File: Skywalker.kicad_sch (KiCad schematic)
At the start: 54 parts

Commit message: no message
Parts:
- removed Pn_Sol1, nO_Sol5: ~, symbol PID_symbols:Solenoid
- removed T2: ~, symbol PID_symbols:Tank
- added Pn_Sol?: ~, symbol PID_symbols:Pneumatic_Solenoid
- added nC_Sol?: ~, symbol PID_symbols:Normally_Closed_Solenoid
- renumbered EthBuffer to Ethanol, T1 to Ethanol, T1 to N2_Tank, G_Nitrous to Nitrous, T1 to Nitrous
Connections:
- net at N2_Tank.: now also CV5., PT?., Reg1., Reg2.
- net at Engine1.: now also PT1.; no longer PT3.
- net at PT1.: no longer Engine1.
- net at CV4.: now also Hose?.1
- net at Nitrous.: now also nC_Sol?.
- net at QD2.: now also CV6.
- new net: CV4., PT?., Pn_Sol?., Reg2., nO_Sol6., nO_Sol7.
- new net: CV4., Ethanol., MB_V2.
- new net: Engine1., PT3.
- new net: BV1., BV3., Engine1.
- new net: CV3., Ethanol., MB_V1., nO_Sol4.
- new net: CV4., nC_Sol?.
- new net: Burst_Disc1., CV1., Ethanol., PT2., SPRV1., nO_Sol1.
- new net: BV2., CV1., CV2.
- new net: Nitrous., PT?., nO_Sol2.
- new net: 3WayPBall?., Pn_Sol?.
- new net: 3WayPBall?., CV6., Nitrous.
- new net: BV1., Burst_Disc2., CV2., Nitrous., PT4., SPRV2.
- now unconnected: Burst_Disc1., Burst_Disc2., PT2., PT4., PT?., PT?., PT?.
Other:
- note added: "Buffer"
- note added: "Gaseous"
- note added: "Main"
- moved on the sheet: N2_Tank, PT?

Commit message: update
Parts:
- gave numbers to parts that had none: 13
- renumbered BV1 to BV2, BV2 to BV3, BV3 to BV4, BV1 to BV5, CV6 to CV10, CV1 to CV3, CV2 to CV4, CV3 to CV5, CV4 to CV6, CV3 to CV7, CV4 to CV8, CV5 to CV9, Ethanol to Fuel1, Ethanol to Ig_Fuel1, Nitrous to Ig_Ox1, MB_V1 to MB_V2, MB_V2 to MB_V3, N2_Tank to N2_Tank1, Nitrous to Ox1, PT4 to PT10, PT1 to PT5, PT2 to PT6, PT3 to PT9, nO_Sol6 to nO_Sol5, nO_Sol7 to nO_Sol6
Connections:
- net at N2_Tank1.: now also CV9., PT7., Reg1., Reg2.
- net at Engine1.: now also PT5.; no longer PT9.
- net at PT5.: no longer Engine1.
- net at CV8.: now also Hose4.1; no longer nC_Sol1.
- net at QD2.: now also CV10.
- new net: CV6., PT13., Pn_Sol1., Reg2., nO_Sol5., nO_Sol6.
- new net: CV6., Ig_Fuel1., MB_V3.
- new net: Engine1., PT9.
- new net: BV2., BV4., Engine1.
- new net: CV5., Ig_Fuel1., MB_V2., nO_Sol4.
- new net: CV8., nC_Sol1.
- new net: Burst_Disc1., CV3., Fuel1., PT6., SPRV1., nO_Sol1.
- new net: BV3., CV3., CV4.
- new net: Ig_Ox1., PT12., nO_Sol2.
- new net: 3WayPBall1., CV10., Ox1.
- new net: BV5., Burst_Disc2., CV4., Ox1., PT10., SPRV2.
- now unconnected: Burst_Disc1., Burst_Disc2., PT10., PT12., PT13., PT6., PT7.

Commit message: legend
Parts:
- removed MB_V1: ~, symbol PID_symbols:MBallValve
- removed Pn_Sol1: ~, symbol PID_symbols:Pneumatic_Solenoid
- added MB_V?: ~, symbol PID_symbols:MBallValve
- added Pn_Sol?: ~, symbol PID_symbols:Pneumatic_Solenoid
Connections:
- net at N2_Tank1.: now also CV9., PT7., Reg1., Reg2.
- net at Engine1.: now also PT5.; no longer PT9.
- net at PT5.: no longer Engine1.
- net at CV8.: now also Hose4.1; no longer nC_Sol1.
- net at CV5., Fuel1., Hose1.1: now also MB_V?.
- net at QD2.: now also CV10.
- new net: CV6., PT13., Pn_Sol?., Reg2., nO_Sol5., nO_Sol6.
- new net: CV6., Ig_Fuel1., MB_V3.
- new net: Engine1., PT9.
- new net: BV2., BV4., Engine1.
- new net: CV5., Ig_Fuel1., MB_V2., nO_Sol4.
- new net: CV8., nC_Sol1.
- new net: Burst_Disc1., CV3., Fuel1., PT6., SPRV1., nO_Sol1.
- new net: BV3., CV3., CV4.
- new net: Ig_Ox1., PT12., nO_Sol2.
- new net: 3WayPBall1., Pn_Sol?.
- new net: 3WayPBall1., CV10., Ox1.
- new net: BV5., Burst_Disc2., CV4., Ox1., PT10., SPRV2.
- now unconnected: Burst_Disc1., Burst_Disc2., PT10., PT12., PT13., PT6., PT7.
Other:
- note added: "1/2" Pipe"
- note added: "1/4" Pipe"
- note added: "LEGEND"
- note added: "Tubing"
- moved on the sheet: Burst_Disc1, CV7, CV8, Hose3, Hose4, PT11, T_I1, nC_Sol1, nO_Sol4

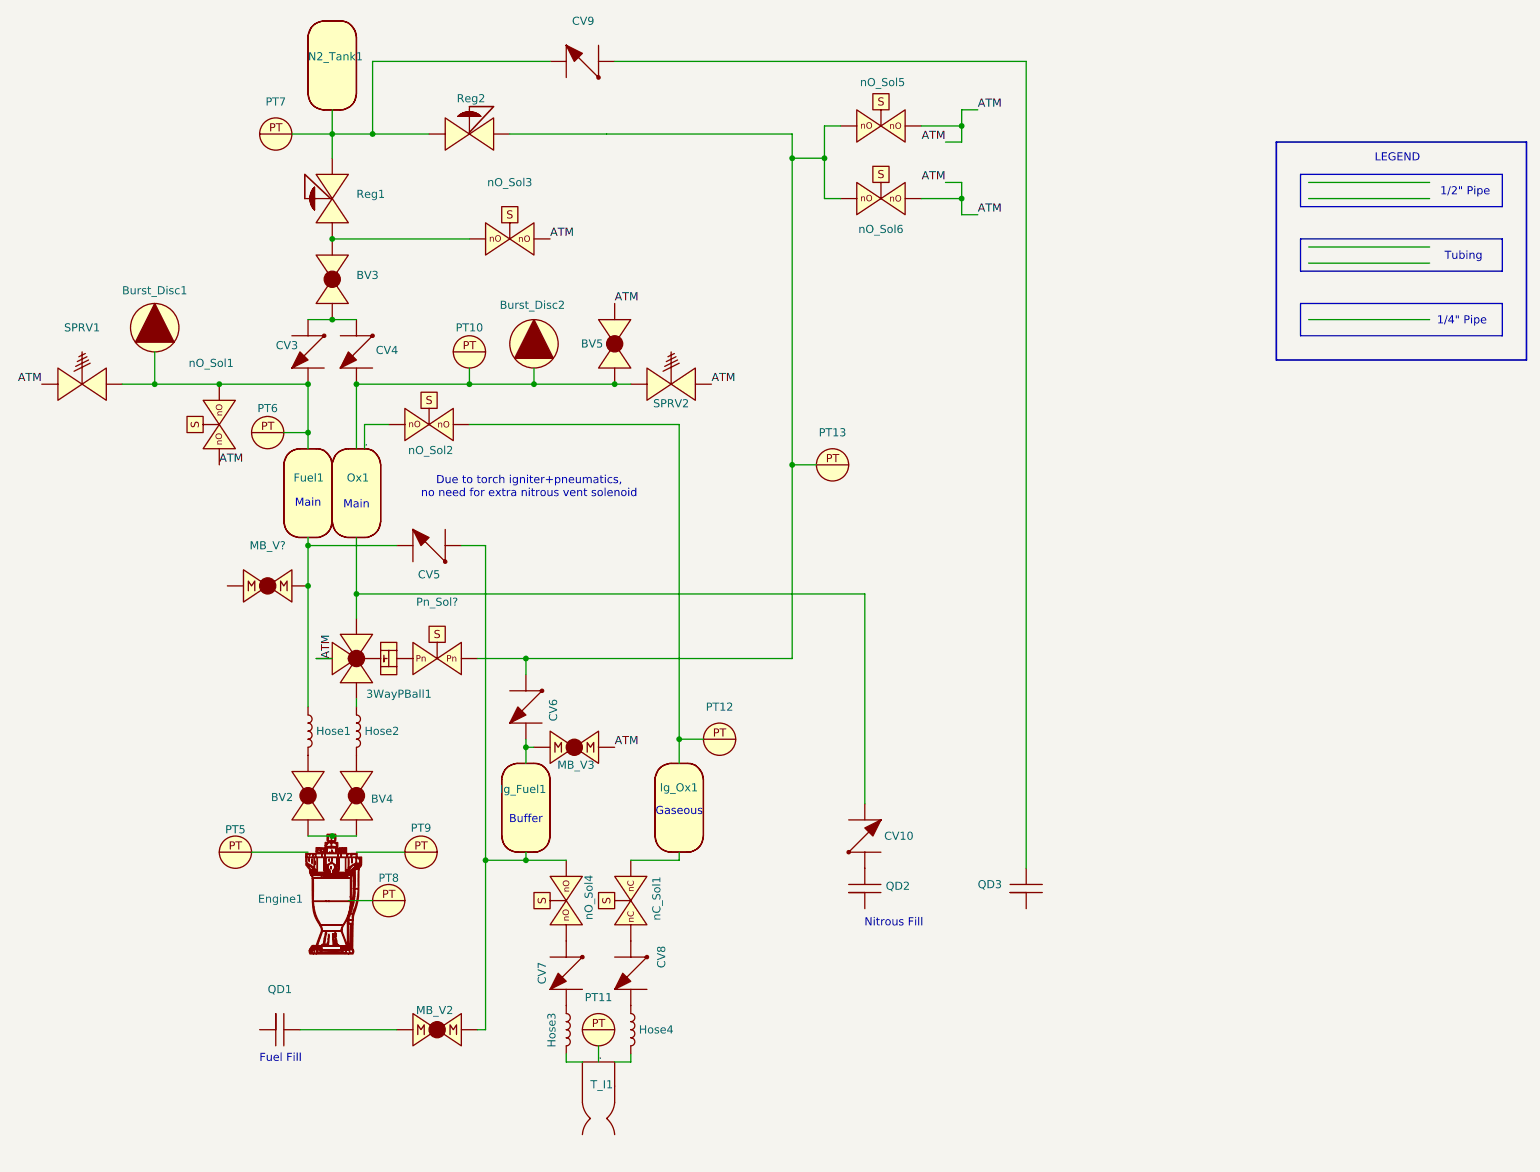
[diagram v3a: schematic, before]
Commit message: added L9 P&ID from Babs, he had problems using git
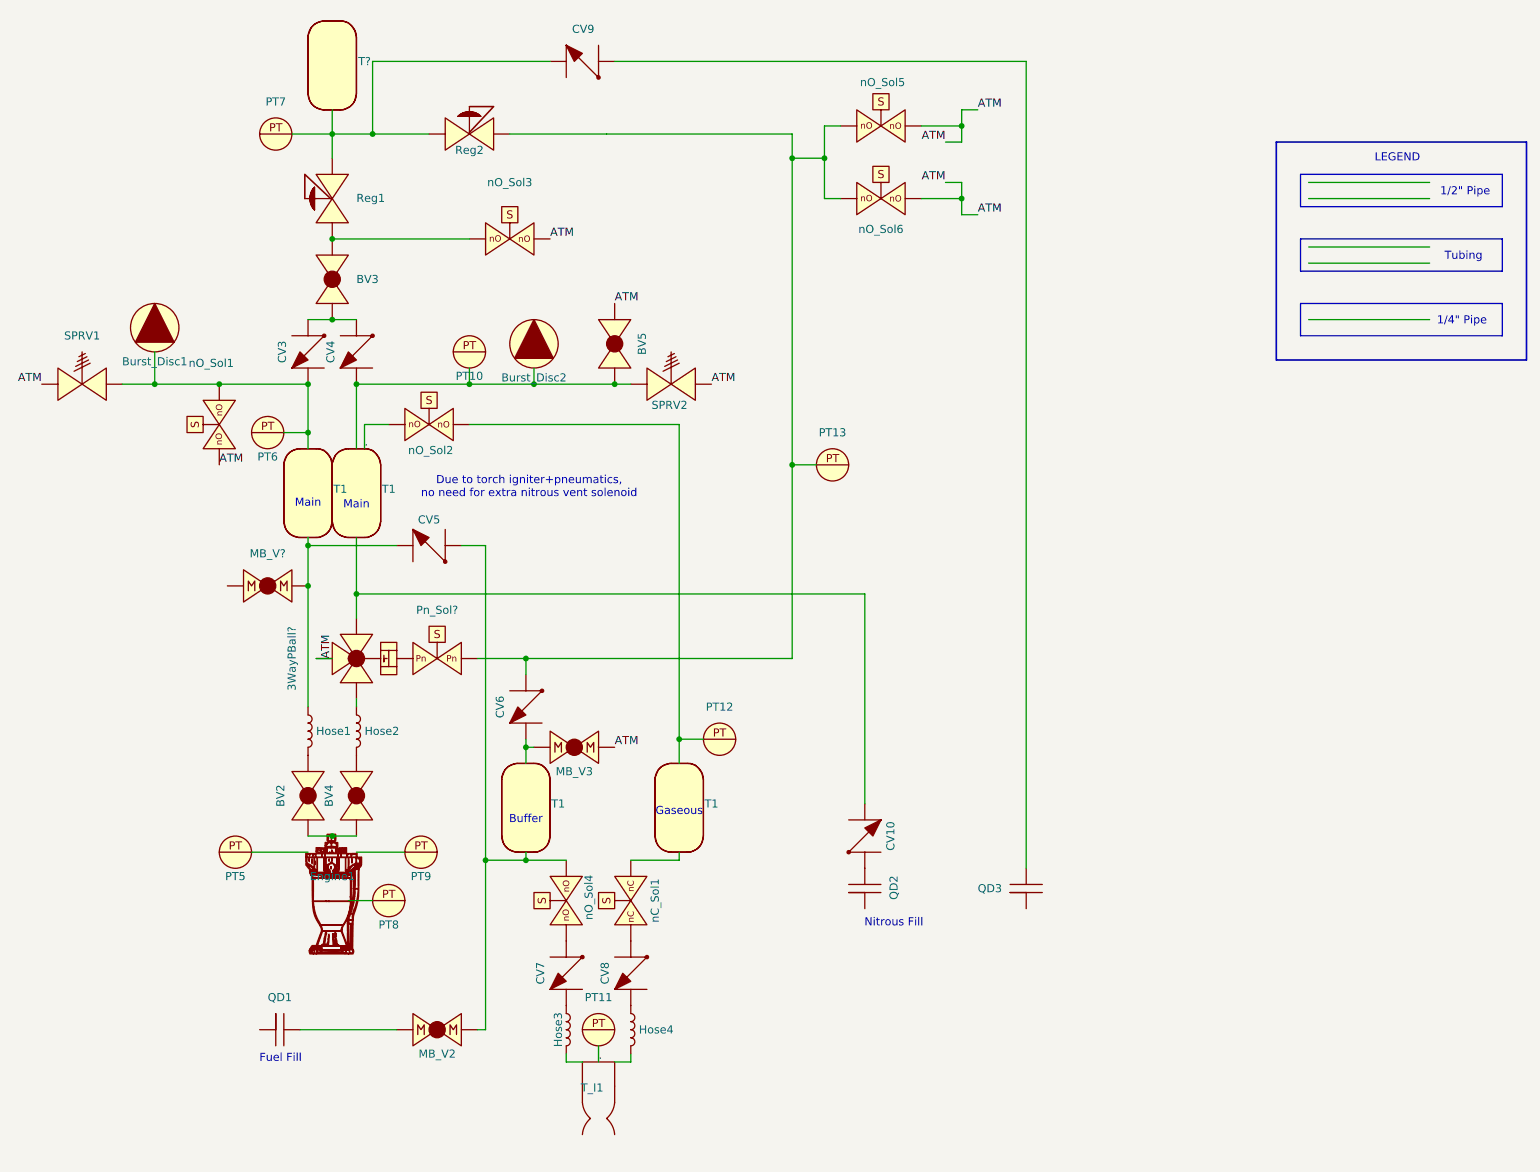
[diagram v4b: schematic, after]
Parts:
- 3WayPBall?: renamed from 3WayPBall1; value ~ -> (none)
- BV2, BV3, BV4, BV5, Burst_Disc1, Burst_Disc2, CV10, CV3, CV4, CV5, CV6, CV7, CV8, CV9, Engine1, Hose1, Hose2, Hose3, Hose4, MB_V2, MB_V3, MB_V?, PT10, PT11, PT12, PT13, PT5, PT6, PT7, PT8, PT9, Pn_Sol?, QD1, QD2, QD3, Reg1, Reg2, SPRV1, SPRV2, T_I1, nC_Sol1: value ~ -> (none)
- T1: renamed from Ig_Fuel1; value ~ -> (none)
- T1: renamed from Ig_Ox1; value ~ -> (none)
- T1: renamed from Fuel1; value ~ -> (none)
- T1: renamed from Ox1; value ~ -> (none)
- T?: renamed from N2_Tank1; value ~ -> (none)
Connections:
- net at T?.: now also CV9., PT7., Reg1., Reg2.
- net at Engine1.: now also PT5.; no longer PT9.
- net at PT5.: no longer Engine1.
- net at CV8.: now also Hose4.1; no longer nC_Sol1.
- net at QD2.: now also CV10.
- new net: CV6., PT13., Pn_Sol?., Reg2., nO_Sol5., nO_Sol6.
- new net: CV6., MB_V3., T1.
- new net: Engine1., PT9.
- new net: BV2., BV4., Engine1.
- new net: CV5., MB_V2., T1., nO_Sol4.
- new net: CV8., nC_Sol1.
- new net: Burst_Disc1., CV3., PT6., SPRV1., T1., nO_Sol1.
- new net: BV3., CV3., CV4.
- new net: PT12., T1., nO_Sol2.
- new net: 3WayPBall?., CV10., T1.
- new net: BV5., Burst_Disc2., CV4., PT10., SPRV2., T1.
- now unconnected: Burst_Disc1., Burst_Disc2., PT10., PT12., PT13., PT6., PT7.

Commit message: okokok
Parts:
- 3WayPBall1: renamed from 3WayPBall?; value (none) -> ~
- BV2, BV3, BV4, BV5, Burst_Disc1, Burst_Disc2, CV10, CV3, CV4, CV5, CV6, CV7, Engine1, Hose1, Hose2, Hose3, Hose4, MB_V2, MB_V3, PT10, PT11, PT12, PT13, PT5, PT6, PT7, PT8, PT9, QD1, QD2, QD3, Reg1, Reg2, SPRV1, SPRV2, T_I1, nC_Sol1: value (none) -> ~
- CV8: renamed from CV9; value (none) -> ~
- CV9: renamed from CV8; value (none) -> ~
- Fuel, Ox: renamed from T1; value (none) -> ~
- MB_V1: renamed from MB_V?; value (none) -> ~
- N1: renamed from T?; value (none) -> ~
- Pn_Sol1: renamed from Pn_Sol?; value (none) -> ~
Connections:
- net at N1.: now also CV8., PT7., Reg1., Reg2.
- net at Engine1.: now also PT5.; no longer PT9.
- net at PT5.: no longer Engine1.
- net at CV9.: now also Hose4.1; no longer nC_Sol1.
- net at QD2.: now also CV10.
- new net: CV6., PT13., Pn_Sol1., Reg2., nO_Sol5., nO_Sol6.
- new net: CV6., Fuel., MB_V3.
- new net: Engine1., PT9.
- new net: BV2., BV4., Engine1.
- new net: CV5., Fuel., MB_V2., nO_Sol4.
- new net: CV9., nC_Sol1.
- new net: Burst_Disc1., CV3., Fuel., PT6., SPRV1., nO_Sol1.
- new net: BV3., CV3., CV4.
- new net: Ox., PT12., nO_Sol2.
- new net: 3WayPBall1., CV10., Ox.
- new net: BV5., Burst_Disc2., CV4., Ox., PT10., SPRV2.
- now unconnected: Burst_Disc1., Burst_Disc2., PT10., PT12., PT13., PT6., PT7.
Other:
- note removed: "1/2" Pipe"
- note removed: "1/4" Pipe"
- note removed: "LEGEND"
- note removed: "Tubing"
- moved on the sheet: Burst_Disc2, PT10

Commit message: no message
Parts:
- renumbered Fuel to Fuel1, Fuel to Fuel2, Ox to Ox1, Ox to Ox2
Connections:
- net at N1.: now also CV8., PT7., Reg1., Reg2.
- net at Engine1.: now also PT5.; no longer PT9.
- net at PT5.: no longer Engine1.
- net at CV9.: now also Hose4.1; no longer nC_Sol1.
- net at QD2.: now also CV10.
- new net: CV6., PT13., Pn_Sol1., Reg2., nO_Sol5., nO_Sol6.
- new net: CV6., Fuel2., MB_V3.
- new net: Engine1., PT9.
- new net: BV2., BV4., Engine1.
- new net: CV5., Fuel2., MB_V2., nO_Sol4.
- new net: CV9., nC_Sol1.
- new net: Burst_Disc1., CV3., Fuel1., PT6., SPRV1., nO_Sol1.
- new net: BV3., CV3., CV4.
- new net: Ox2., PT12., nO_Sol2.
- new net: 3WayPBall1., CV10., Ox1.
- new net: BV5., Burst_Disc2., CV4., Ox1., PT10., SPRV2.
- now unconnected: Burst_Disc1., Burst_Disc2., PT10., PT12., PT13., PT6., PT7.
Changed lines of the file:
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@@
 		(on_board yes)
 		(dnp no)
-		(property "Reference" "Fuel"
+		(property "Reference" "Fuel2"
 			(at 93.726 138.43 0)
 			(effects
@@
 			(project "P_IDs"
 				(path "/045f1f05-3134-4b6d-91b6-463031104f1e/8ff5724e-b29b-49c2-a1fa-190081404476"
-					(reference "Fuel")
+					(reference "Fuel2")
 					(unit 1)
 				)
@@
 		(on_board yes)
 		(dnp no)
-		(property "Reference" "Ox"
+		(property "Reference" "Ox2"
 			(at 116.84 138.176 0)
 			(effects
@@
 			(project "P_IDs"
 				(path "/045f1f05-3134-4b6d-91b6-463031104f1e/8ff5724e-b29b-49c2-a1fa-190081404476"
-					(reference "Ox")
+					(reference "Ox2")
 					(unit 1)
 				)
@@
 		(on_board yes)
 		(dnp no)
-		(property "Reference" "Fuel"
+		(property "Reference" "Fuel1"
 			(at 59.182 88.646 0)
 			(effects
@@
 			(project "P_IDs"
 				(path "/045f1f05-3134-4b6d-91b6-463031104f1e/8ff5724e-b29b-49c2-a1fa-190081404476"
-					(reference "Fuel")
+					(reference "Fuel1")
 					(unit 1)
 				)
@@
 		(on_board yes)
 		(dnp no)
-		(property "Reference" "Ox"
+		(property "Reference" "Ox1"
 			(at 67.31 88.646 0)
 			(effects
@@
 			(project "P_IDs"
 				(path "/045f1f05-3134-4b6d-91b6-463031104f1e/8ff5724e-b29b-49c2-a1fa-190081404476"
-					(reference "Ox")
-					(unit 1)
-				)
+					(reference "Ox1")
+					(unit 1)
+				)

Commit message: no message
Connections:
- net at N1.: now also CV8., PT7., Reg1., Reg2.
- net at Engine1.: now also PT5.; no longer PT9.
- net at PT5.: no longer Engine1.
- net at CV9.: now also Hose4.1; no longer nC_Sol1.
- net at QD2.: now also CV10.
- new net: CV6., PT13., Pn_Sol1., Reg2., nO_Sol5., nO_Sol6.
- new net: CV6., Fuel2., MB_V3.
- new net: Engine1., PT9.
- new net: BV2., BV4., Engine1.
- new net: CV5., Fuel2., MB_V2., nO_Sol4.
- new net: CV9., nC_Sol1.
- new net: Burst_Disc1., CV3., Fuel1., PT6., SPRV1., nO_Sol1.
- new net: BV3., CV3., CV4.
- new net: Ox2., PT12., nO_Sol2.
- new net: 3WayPBall1., CV10., Ox1.
- new net: BV5., Burst_Disc2., CV4., Ox1., PT10., SPRV2.
- now unconnected: Burst_Disc1., Burst_Disc2., PT10., PT12., PT13., PT6., PT7.
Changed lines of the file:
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@@
 	(wire
 		(pts
+			(xy 87.63 148.59) (xy 93.98 148.59)
+		)
+		(stroke
+			(width 0)
+			(type solid)
+			(color 255 255 255 1)
+		)
+	)
+	(wire
+		(pts
 			(xy 100.33 148.59) (xy 93.98 148.59)
 		)
@@
 	(wire
 		(pts
-			(xy 87.63 148.59) (xy 93.98 148.59)
-		)
-		(stroke
-			(width 0)
-			(type solid)
-			(color 255 255 255 1)
-		)
-	)
-	(wire
-		(pts
 			(xy 140.97 33.02) (xy 143.51 33.02)
 		)
@@
 	)
 	(symbol
-		(lib_name "PID_symbols:Tank")
 		(lib_id "PID_symbols:Tank")
 		(at 62.23 27.94 0)
@@
 	)
 	(symbol
-		(lib_name "PID_symbols:Check_Valve")
 		(lib_id "PID_symbols:Check_Valve")
 		(at 93.98 121.92 270)
@@
 	)
 	(symbol
-		(lib_name "PID_symbols:Pressure_Transducer")
 		(lib_id "PID_symbols:Pressure_Transducer")
 		(at 72.39 154.94 0)
@@
 	)
 	(symbol
-		(lib_name "PID_symbols:Pressure_Transducer")
 		(lib_id "PID_symbols:Pressure_Transducer")
 		(at 77.47 147.32 0)
@@
 	)
 	(symbol
-		(lib_name "PID_symbols:Check_Valve")
 		(lib_id "PID_symbols:Check_Valve")
 		(at 105.41 22.86 180)
@@
 	)
 	(symbol
-		(lib_name "PID_symbols:MBallValve")
 		(lib_id "PID_symbols:MBallValve")
 		(at 80.01 175.26 0)
@@
 	)
 	(symbol
-		(lib_name "PID_symbols:Ball_Valve")
 		(lib_id "PID_symbols:Ball_Valve")
 		(at 67.31 134.62 270)
@@
 	)
 	(symbol
-		(lib_name "PID_symbols:Check_Valve")
 		(lib_id "PID_symbols:Check_Valve")
 		(at 110.49 163.83 270)
@@
 	)
 	(symbol
-		(lib_name "PID_symbols:Check_Valve")
 		(lib_id "PID_symbols:Check_Valve")
 		(at 59.69 66.04 270)
@@
 	)
 	(symbol
-		(lib_name "PID_symbols:Pressure_Regulator")
 		(lib_id "PID_symbols:Pressure_Regulator")
 		(at 81.28 34.29 0)
@@
 	)
 	(symbol
-		(lib_name "PID_symbols:Pressure_Transducer")
 		(lib_id "PID_symbols:Pressure_Transducer")
 		(at 53.34 81.28 0)
@@
 	)
 	(symbol
-		(lib_name "PID_symbols:Tank")
 		(lib_id "PID_symbols:Tank")
 		(at 92.71 144.78 0)
@@
 	)
 	(symbol
-		(lib_name "PID_symbols:Tank")
 		(lib_id "PID_symbols:Tank")
 		(at 116.84 144.78 0)
@@
 	)
 	(symbol
-		(lib_name "PID_symbols:Check_Valve")
 		(lib_id "PID_symbols:Check_Valve")
 		(at 100.33 163.83 270)
@@
 	)
 	(symbol
-		(lib_name "PID_symbols:Tank")
 		(lib_id "PID_symbols:Tank")
 		(at 58.42 95.25 0)
@@
 	)
 	(symbol
-		(lib_name "PID_symbols:Pressure_Transducer")
 		(lib_id "PID_symbols:Pressure_Transducer")
 		(at 48.26 147.32 0)
@@
 	)
 	(symbol
-		(lib_name "PID_symbols:Solenoid")
 		(lib_id "PID_symbols:Solenoid")
 		(at 146.05 33.02 0)
@@
 	)
 	(symbol
-		(lib_name "PID_symbols:Quick_Disconnect")
 		(lib_id "PID_symbols:Quick_Disconnect")
 		(at 172.72 153.67 90)
@@
 	)
 	(symbol
-		(lib_name "PID_symbols:Ball_Valve")
 		(lib_id "PID_symbols:Ball_Valve")
 		(at 107.95 71.12 90)
@@
 	)
 	(symbol
-		(lib_name "PID_symbols:Solenoid")
 		(lib_id "PID_symbols:Solenoid")
 		(at 74.93 80.01 0)
@@
 	)
 	(symbol
-		(lib_name "PID_symbols:Quick_Disconnect")
 		(lib_id "PID_symbols:Quick_Disconnect")
 		(at 54.61 175.26 0)
@@
 	)
 	(symbol
-		(lib_name "PID_symbols:Quick_Disconnect")
 		(lib_id "PID_symbols:Quick_Disconnect")
 		(at 147.32 153.67 90)
@@
 	)
 	(symbol
-		(lib_name "PID_symbols:Ball_Valve")
 		(lib_id "PID_symbols:Ball_Valve")
 		(at 63.5 60.96 90)
@@
 	)
 	(symbol
-		(lib_name "PID_symbols:SPRV")
 		(lib_id "PID_symbols:SPRV")
 		(at 20.32 73.66 0)
@@
 	)
 	(symbol
-		(lib_name "PID_symbols:Pressure_Transducer")
 		(lib_id "PID_symbols:Pressure_Transducer")
 		(at 124.46 129.54 0)
@@
 	)
 	(symbol
-		(lib_name "PID_symbols:Solenoid")
 		(lib_id "PID_symbols:Solenoid")
 		(at 87.63 50.8 0)
@@
 	)
 	(symbol
-		(lib_name "PID_symbols:Pressure_Transducer")
 		(lib_id "PID_symbols:Pressure_Transducer")
 		(at 142.24 86.36 0)
@@
 	)
 	(symbol
-		(lib_name "PID_symbols:Pressure_Transducer")
 		(lib_id "PID_symbols:Pressure_Transducer")
 		(at 105.41 175.26 0)
@@
 	)
 	(symbol
-		(lib_name "PID_symbols:Pressure_Regulator")
 		(lib_id "PID_symbols:Pressure_Regulator")
 		(at 63.5 48.26 90)
@@
 	)
 	(symbol
-		(lib_name "PID_symbols:Pressure_Transducer")
 		(lib_id "PID_symbols:Pressure_Transducer")
 		(at 54.61 34.29 0)
@@
 	)
 	(symbol
-		(lib_name "PID_symbols:Ball_Valve")
 		(lib_id "PID_symbols:Ball_Valve")
 		(at 59.69 134.62 270)
@@
 	)
 	(symbol
-		(lib_name "PID_symbols:SPRV")
 		(lib_id "PID_symbols:SPRV")
 		(at 113.03 73.66 0)
@@
 	)
 	(symbol
-		(lib_name "PID_symbols:Check_Valve")
 		(lib_id "PID_symbols:Check_Valve")
 		(at 81.28 99.06 180)
@@
 	)
 	(symbol
-		(lib_name "PID_symbols:Check_Valve")
 		(lib_id "PID_symbols:Check_Valve")
 		(at 147.32 147.32 90)
@@
 	)
 	(symbol
-		(lib_name "PID_symbols:Tank")
 		(lib_id "PID_symbols:Tank")
 		(at 66.04 95.25 0)
@@
 	)
 	(symbol
-		(lib_name "PID_symbols:Burst_Disc")
 		(lib_id "PID_symbols:Burst_Disc")
 		(at 95.25 66.04 0)
@@
 	)
 	(symbol
-		(lib_name "PID_symbols:MBallValve")
 		(lib_id "PID_symbols:MBallValve")
 		(at 53.34 105.41 0)
@@
 	)
 	(symbol
-		(lib_name "PID_symbols:Pressure_Transducer")
 		(lib_id "PID_symbols:Pressure_Transducer")
 		(at 86.36 68.58 0)
@@
 	)
 	(symbol
-		(lib_name "PID_symbols:MBallValve")
 		(lib_id "PID_symbols:MBallValve")
 		(at 101.6 130.81 0)
@@
 	)
 	(symbol
-		(lib_name "PID_symbols:Solenoid")
 		(lib_id "PID_symbols:Solenoid")
 		(at 100.33 158.75 90)
@@
 	)
 	(symbol
-		(lib_name "PID_symbols:Solenoid")
 		(lib_id "PID_symbols:Solenoid")
 		(at 146.05 44.45 0)
@@
 	)
 	(symbol
-		(lib_name "PID_symbols:Burst_Disc")
 		(lib_id "PID_symbols:Burst_Disc")
 		(at 35.56 64.77 0)
@@
 	)
 	(symbol
-		(lib_name "PID_symbols:Solenoid")
 		(lib_id "PID_symbols:Solenoid")
 		(at 45.72 83.82 90)
@@
 	)
 	(symbol
-		(lib_name "PID_symbols:Check_Valve")
 		(lib_id "PID_symbols:Check_Valve")
 		(at 67.31 66.04 270)

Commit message: for sahil
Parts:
- renumbered BV3 to BV2, BV5 to BV3, BV2 to BV4, BV4 to BV5, CV9 to CV10, CV8 to CV3, CV3 to CV4, CV4 to CV5, CV5 to CV6, CV6 to CV7, CV10 to CV8, CV7 to CV9, MB_V3 to MB_V2, MB_V2 to MB_V3, PT5 to PT10, PT9 to PT11, PT8 to PT12, PT11 to PT13, PT7 to PT5, PT10 to PT6, PT6 to PT7, PT13 to PT8, PT12 to PT9, QD2 to QD1, QD3 to QD2, QD1 to QD3, Reg2 to Reg1, Reg1 to Reg2, nO_Sol5 to nO_Sol1, nO_Sol6 to nO_Sol2, nO_Sol2 to nO_Sol4, nO_Sol1 to nO_Sol5, nO_Sol4 to nO_Sol6
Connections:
- net at N1.: now also CV3., PT5., Reg1., Reg2.
- net at Engine1.: now also PT10.; no longer PT11.
- net at PT10.: no longer Engine1.
- net at CV10.: now also Hose4.1; no longer nC_Sol1.
- net at QD1.: now also CV8.
- new net: CV7., PT8., Pn_Sol1., Reg1., nO_Sol1., nO_Sol2.
- new net: CV7., Fuel2., MB_V2.
- new net: Engine1., PT11.
- new net: BV4., BV5., Engine1.
- new net: CV6., Fuel2., MB_V3., nO_Sol6.
- new net: CV10., nC_Sol1.
- new net: Burst_Disc1., CV4., Fuel1., PT7., SPRV1., nO_Sol5.
- new net: BV2., CV4., CV5.
- new net: Ox2., PT9., nO_Sol4.
- new net: 3WayPBall1., CV8., Ox1.
- new net: BV3., Burst_Disc2., CV5., Ox1., PT6., SPRV2.
- now unconnected: Burst_Disc1., Burst_Disc2., PT5., PT6., PT7., PT8., PT9.
